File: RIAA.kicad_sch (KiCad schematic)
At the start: 114 parts, among them K1 G6K-2, P11 From Keyboard, P8 From main PCB, P9 From Wire, U1 OPA2134, U2 OPA2134, U3 LM317_TO-220, U4 LM337_TO-220, U5 OPA2134, U6 OPA2134, U7 LM317_TO-220

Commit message: WIP: Added gerber files.
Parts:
- added C108, C208: 10uF, Capacitor_THT:CP_Radial_D5.0mm_P2.50mm, symbol Device:C_Polarized_Small
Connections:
- net GND: now also C108.2, C208.2; no longer R110.2, R210.2
- new net: C208.1, R210.2
- new net: C108.1, R110.2
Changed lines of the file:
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@@
 	(wire
 		(pts
-			(xy 372.11 106.68) (xy 372.11 105.41)
-		)
-		(stroke
-			(width 0)
-			(type default)
-		)
-	)
-	(wire
-		(pts
 			(xy -83.82 73.66) (xy -87.63 73.66)
 		)
@@
 	(wire
 		(pts
+			(xy 58.42 180.34) (xy 64.77 180.34)
+		)
+		(stroke
+			(width 0)
+			(type default)
+		)
+	)
+	(wire
+		(pts
 			(xy 93.98 170.18) (xy 93.98 168.91)
 		)
@@
 	(wire
 		(pts
-			(xy 220.98 180.34) (xy 220.98 186.69)
+			(xy 190.5 113.03) (xy 190.5 115.57)
 		)
 		(stroke
@@
 	(wire
 		(pts
-			(xy 190.5 106.68) (xy 190.5 105.41)
+			(xy 220.98 180.34) (xy 220.98 186.69)
 		)
 		(stroke
@@
 	(wire
 		(pts
+			(xy 190.5 105.41) (xy 190.5 107.95)
+		)
+		(stroke
+			(width 0)
+			(type default)
+		)
+	)
+	(wire
+		(pts
 			(xy -228.6 49.53) (xy -222.25 49.53)
 		)
@@
 	(wire
 		(pts
+			(xy 372.11 111.76) (xy 372.11 114.3)
+		)
+		(stroke
+			(width 0)
+			(type default)
+		)
+	)
+	(wire
+		(pts
 			(xy 372.11 95.25) (xy 378.46 95.25)
 		)
@@
 	(wire
 		(pts
+			(xy 372.11 105.41) (xy 372.11 106.68)
+		)
+		(stroke
+			(width 0)
+			(type default)
+		)
+	)
+	(wire
+		(pts
 			(xy 393.7 149.86) (xy 393.7 162.56)
 		)
@@
 	(wire
 		(pts
-			(xy 58.42 180.34) (xy 64.77 180.34)
-		)
-		(stroke
-			(width 0)
-			(type default)
-		)
-	)
-	(wire
-		(pts
 			(xy 247.65 138.43) (xy 254 138.43)
 		)
@@
 				(size 1.27 1.27)
 			)
-			(justify left top)
+			(justify right top)
 		)
 	)
@@
 	)
 	(symbol
+		(lib_id "Device:C_Polarized_Small")
+		(at 372.11 109.22 0)
+		(unit 1)
+		(exclude_from_sim no)
+		(in_bom yes)
+		(on_board yes)
+		(dnp no)
+		(fields_autoplaced yes)
+		(property "Reference" "C208"
+			(at 374.65 107.4038 0)
+			(effects
+				(font
+					(size 1.27 1.27)
+				)
+				(justify left)
+			)
+		)
+		(property "Value" "10uF"
+			(at 374.65 109.9438 0)
+			(effects
+				(font
+					(size 1.27 1.27)
+				)
+				(justify left)
+			)
+		)
+		(property "Footprint" "Capacitor_THT:CP_Radial_D5.0mm_P2.50mm"
+			(at 372.11 109.22 0)
+			(effects
+				(font
+					(size 1.27 1.27)
+				)
+				(hide yes)
+			)
+		)
+		(property "Datasheet" "~"
+			(at 372.11 109.22 0)
+			(effects
+				(font
+					(size 1.27 1.27)
+				)
+				(hide yes)
+			)
+		)
+		(property "Description" "Polarized capacitor, small symbol"
+			(at 372.11 109.22 0)
+			(effects
+				(font
+					(size 1.27 1.27)
+				)
+				(hide yes)
+			)
+		)
+		(pin "2"
+		)
+		(pin "1"
+		)
+		(instances
+			(project "RIAA"
+				(path "/d42afdab-200b-47bd-9783-ae2fad19e73b"
+					(reference "C208")
+					(unit 1)
+				)
+			)
+		)
+	)
+	(symbol
 		(lib_id "Device:R")
 		(at 77.47 175.26 0)
@@
 	(symbol
 		(lib_id "power:GND")
-		(at 372.11 106.68 0)
+		(at 372.11 114.3 0)
+		(mirror y)
 		(unit 1)
 		(exclude_from_sim no)
@@
 		(on_board yes)
 		(dnp no)
-		(fields_autoplaced yes)
 		(property "Reference" "#PWR022"
-			(at 372.11 113.03 0)
+			(at 372.11 120.65 0)
 			(effects
 				(font
@@
 		)
 		(property "Value" "GND"
-			(at 372.11 111.76 0)
+			(at 372.11 119.38 0)
 			(effects
 				(font
@@
 		)
 		(property "Footprint" ""
-			(at 372.11 106.68 0)
+			(at 372.11 114.3 0)
 			(effects
 				(font
@@
 		)
 		(property "Datasheet" ""
-			(at 372.11 106.68 0)
+			(at 372.11 114.3 0)
 			(effects
 				(font
@@
 		)
 		(property "Description" "Power symbol creates a global label with name \"GND\" , ground"
-			(at 372.11 106.68 0)
+			(at 372.11 114.3 0)
 			(effects
 				(font
@@
 	(symbol
 		(lib_id "power:GND")
-		(at 190.5 106.68 0)
+		(at 190.5 115.57 0)
+		(mirror y)
 		(unit 1)
 		(exclude_from_sim no)
@@
 		(on_board yes)
 		(dnp no)
-		(fields_autoplaced yes)
 		(property "Reference" "#PWR015"
-			(at 190.5 113.03 0)
+			(at 190.5 121.92 0)
 			(effects
 				(font
@@
 		)
 		(property "Value" "GND"
-			(at 190.5 111.76 0)
+			(at 190.5 120.65 0)
 			(effects
 				(font
@@
 		)
 		(property "Footprint" ""
-			(at 190.5 106.68 0)
+			(at 190.5 115.57 0)
 			(effects
 				(font
@@
 		)
 		(property "Datasheet" ""
-			(at 190.5 106.68 0)
+			(at 190.5 115.57 0)
 			(effects
 				(font
@@
 		)
 		(property "Description" "Power symbol creates a global label with name \"GND\" , ground"
-			(at 190.5 106.68 0)
+			(at 190.5 115.57 0)
 			(effects
 				(font
@@
 					(unit 1)
 				)
+			)
+		)
+	)
+	(symbol
+		(lib_id "Device:C_Polarized_Small")
+		(at 190.5 110.49 0)
+		(mirror y)
+		(unit 1)
+		(exclude_from_sim no)
+		(in_bom yes)
+		(on_board yes)
+		(dnp no)
+		(property "Reference" "C108"
+			(at 187.96 108.6738 0)
+			(effects
+				(font
+					(size 1.27 1.27)
+				)
+				(justify left)
+			)
+		)
+		(property "Value" "10uF"
+			(at 187.96 111.2138 0)
+			(effects
+				(font
+					(size 1.27 1.27)
+				)
+				(justify left)
+			)
+		)
+		(property "Footprint" "Capacitor_THT:CP_Radial_D5.0mm_P2.50mm"
+			(at 190.5 110.49 0)
+			(effects
+				(font
+					(size 1.27 1.27)
+				)
+				(hide yes)
+			)
+		)
+		(property "Datasheet" "~"
+			(at 190.5 110.49 0)
+			(effects
+				(font
+					(size 1.27 1.27)
+				)
+				(hide yes)
+			)
+		)
+		(property "Description" "Polarized capacitor, small symbol"
+			(at 190.5 110.49 0)
+			(effects
+				(font
+					(size 1.27 1.27)
+				)
+				(hide yes)
+			)
+		)
+		(pin "2"
+		)
+		(pin "1"
+		)
+		(instances
+			(project "RIAA"
+				(path "/d42afdab-200b-47bd-9783-ae2fad19e73b"
+					(reference "C108")
+					(unit 1)
+				)

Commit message: WIP: Started on 3v3 voltage regulator for esp32.
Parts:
- added C34, C35, C36, C37: 22uF, Capacitor_THT:C_Rect_L4.6mm_W3.0mm_P2.50mm_MKS02_FKP02, symbol Device:C
- added L1: 4.7uH, symbol Device:L
- added R23, R25: 470, Resistor_THT:R_Axial_DIN0204_L3.6mm_D1.6mm_P7.62mm_Horizontal, symbol Device:R
- added R24: 6k8, Resistor_THT:R_Axial_DIN0204_L3.6mm_D1.6mm_P7.62mm_Horizontal, symbol Device:R
- added U10: AP63203WU, Package_TO_SOT_SMD:TSOT-23-6, symbol Regulator_Switching:AP63203WU
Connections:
- net 24VDC+: now also C34.2, U10.2 (EN), U10.3 (IN)
- net GND: now also C34.1, C35.1, C36.1, R24.1, U10.4 (GND)
- net R OUT: now also R25.1; no longer C207.2
- new net: C207.2, R23.2, R24.2
- new net: R23.1, R25.2
- new net: C37.1, U10.6 (BST)
- new net: C37.2, L1.1, U10.5 (SW)
- new net 3v3: C35.2, C36.2, L1.2, U10.1 (FB)

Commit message: WIP: Working on SMD version.
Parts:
- removed C34, C35, C36, C37: 22uF, Capacitor_THT:C_Rect_L4.6mm_W3.0mm_P2.50mm_MKS02_FKP02, symbol Device:C
- removed L1: 4.7uH, symbol Device:L
- removed R23, R25: 470, Resistor_THT:R_Axial_DIN0204_L3.6mm_D1.6mm_P7.62mm_Horizontal, symbol Device:R
- removed R24: 6k8, Resistor_THT:R_Axial_DIN0204_L3.6mm_D1.6mm_P7.62mm_Horizontal, symbol Device:R
- removed U10: AP63203WU, Package_TO_SOT_SMD:TSOT-23-6, symbol Regulator_Switching:AP63203WU
- BC1: footprint Package_TO_SOT_THT:TO-92 -> Package_TO_SOT_SMD:SOT-23_Handsoldering
- C204, C205: footprint Capacitor_THT:C_Rect_L4.6mm_W3.0mm_P2.50mm_MKS02_FKP02 -> Capacitor_THT:C_Rect_L7.2mm_W4.5mm_P5.00mm_FKS2_FKP2_MKS2_MKP2
- C206, C207, C208, C29, C30: footprint Capacitor_THT:CP_Radial_D5.0mm_P2.50mm -> Capacitor_SMD:CP_Elec_5x5.4
- C31: footprint Capacitor_THT:CP_Radial_D13.0mm_P7.50mm -> Capacitor_SMD:CP_Elec_8x6.9
- C33: footprint Capacitor_THT:CP_Radial_D8.0mm_P5.00mm -> Capacitor_SMD:CP_Elec_5x5.4
- D5, D6, D7, D8: footprint Diode_THT:D_A-405_P10.16mm_Horizontal -> Diode_SMD:D_MiniMELF
- R19, R20, R202, R203, R204, R205, R206, R208, R209, R21, R210, R211, R212, R22: footprint Resistor_THT:R_Axial_DIN0204_L3.6mm_D1.6mm_P7.62mm_Horizontal -> Resistor_SMD:R_1206_3216Metric_Pad1.30x1.75mm_HandSolder
- R207: footprint Resistor_THT:R_Axial_DIN0204_L3.6mm_D1.6mm_P7.62mm_Horizontal -> Resistor_SMD:R_1206_3216Metric_Pad1.30x1.75mm_HandSolder; LSCSL PN (none) -> C137334
- U7: footprint Package_TO_SOT_THT:TO-220-3_Horizontal_TabDown -> Package_TO_SOT_SMD:TO-252-3_TabPin2
- renumbered P11 to P10
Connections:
- net R OUT: now also C207.2

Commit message: WIP: Working on SMD.
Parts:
- C201, C202, C203: footprint Capacitor_THT:C_Rect_L4.6mm_W3.0mm_P2.50mm_MKS02_FKP02 -> Capacitor_THT:C_Rect_L7.2mm_W4.5mm_P5.00mm_FKS2_FKP2_MKS2_MKP2
- C27, C28, C32: footprint Capacitor_THT:C_Rect_L4.6mm_W3.0mm_P2.50mm_MKS02_FKP02 -> Capacitor_SMD:C_1206_3216Metric_Pad1.33x1.80mm_HandSolder
- C33: footprint Capacitor_SMD:CP_Elec_5x5.4 -> Capacitor_SMD:C_1206_3216Metric_Pad1.33x1.80mm_HandSolder
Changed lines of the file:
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@@
 	(title_block
 		(title "Beogram 4002 RIAA")
-		(date "2024-04-12")
+		(date "2026-27-01")
 		(rev "0.1")
 		(company "LEICHT.IO")
@@
 			)
 		)
-		(property "Footprint" "Capacitor_THT:C_Rect_L4.6mm_W3.0mm_P2.50mm_MKS02_FKP02"
+		(property "Footprint" "Capacitor_THT:C_Rect_L7.2mm_W4.5mm_P5.00mm_FKS2_FKP2_MKS2_MKP2"
 			(at 261.9248 82.55 0)
 			(effects
@@
 			)
 		)
-		(property "Footprint" "Capacitor_THT:C_Rect_L4.6mm_W3.0mm_P2.50mm_MKS02_FKP02"
+		(property "Footprint" "Capacitor_SMD:C_1206_3216Metric_Pad1.33x1.80mm_HandSolder"
 			(at 24.4348 77.47 0)
 			(effects
@@
 			)
 		)
-		(property "Footprint" "Capacitor_THT:C_Rect_L4.6mm_W3.0mm_P2.50mm_MKS02_FKP02"
+		(property "Footprint" "Capacitor_THT:C_Rect_L7.2mm_W4.5mm_P5.00mm_FKS2_FKP2_MKS2_MKP2"
 			(at 293.0652 114.3 0)
 			(effects
@@
 			)
 		)
-		(property "Footprint" "Capacitor_THT:C_Rect_L4.6mm_W3.0mm_P2.50mm_MKS02_FKP02"
+		(property "Footprint" "Capacitor_SMD:C_1206_3216Metric_Pad1.33x1.80mm_HandSolder"
 			(at 40.9448 77.47 0)
 			(effects
@@
 			)
 		)
-		(property "Footprint" "Capacitor_SMD:CP_Elec_5x5.4"
+		(property "Footprint" "Capacitor_SMD:C_1206_3216Metric_Pad1.33x1.80mm_HandSolder"
 			(at 256.54 138.43 0)
 			(effects
@@
 			)
 		)
-		(property "Footprint" "Capacitor_THT:C_Rect_L4.6mm_W3.0mm_P2.50mm_MKS02_FKP02"
+		(property "Footprint" "Capacitor_THT:C_Rect_L7.2mm_W4.5mm_P5.00mm_FKS2_FKP2_MKS2_MKP2"
 			(at 302.26 96.8248 0)
 			(effects
@@
 			)
 		)
-		(property "Footprint" "Capacitor_THT:C_Rect_L4.6mm_W3.0mm_P2.50mm_MKS02_FKP02"
+		(property "Footprint" "Capacitor_SMD:C_1206_3216Metric_Pad1.33x1.80mm_HandSolder"
 			(at 128.5748 167.64 0)
 			(effects

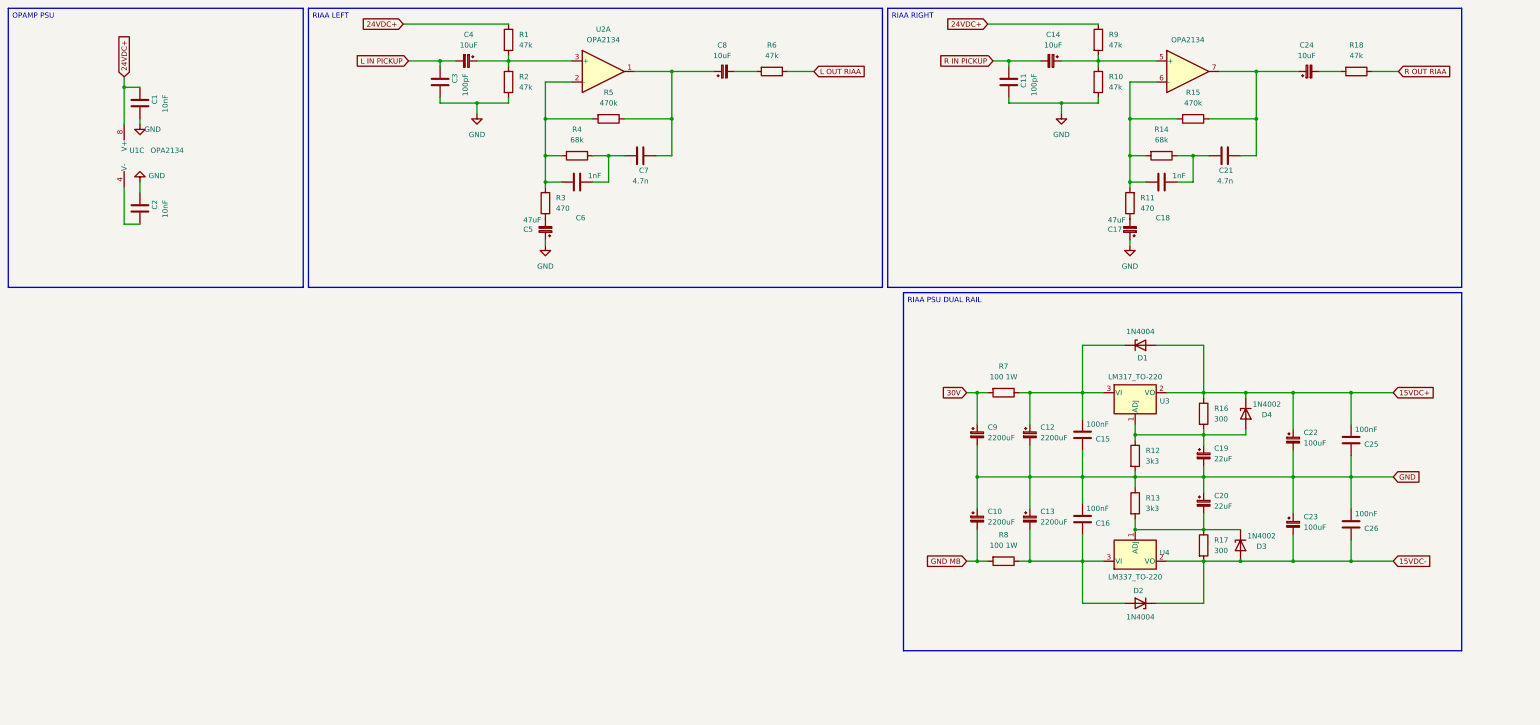
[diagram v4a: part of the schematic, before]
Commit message: WIP: Working on SMD version.
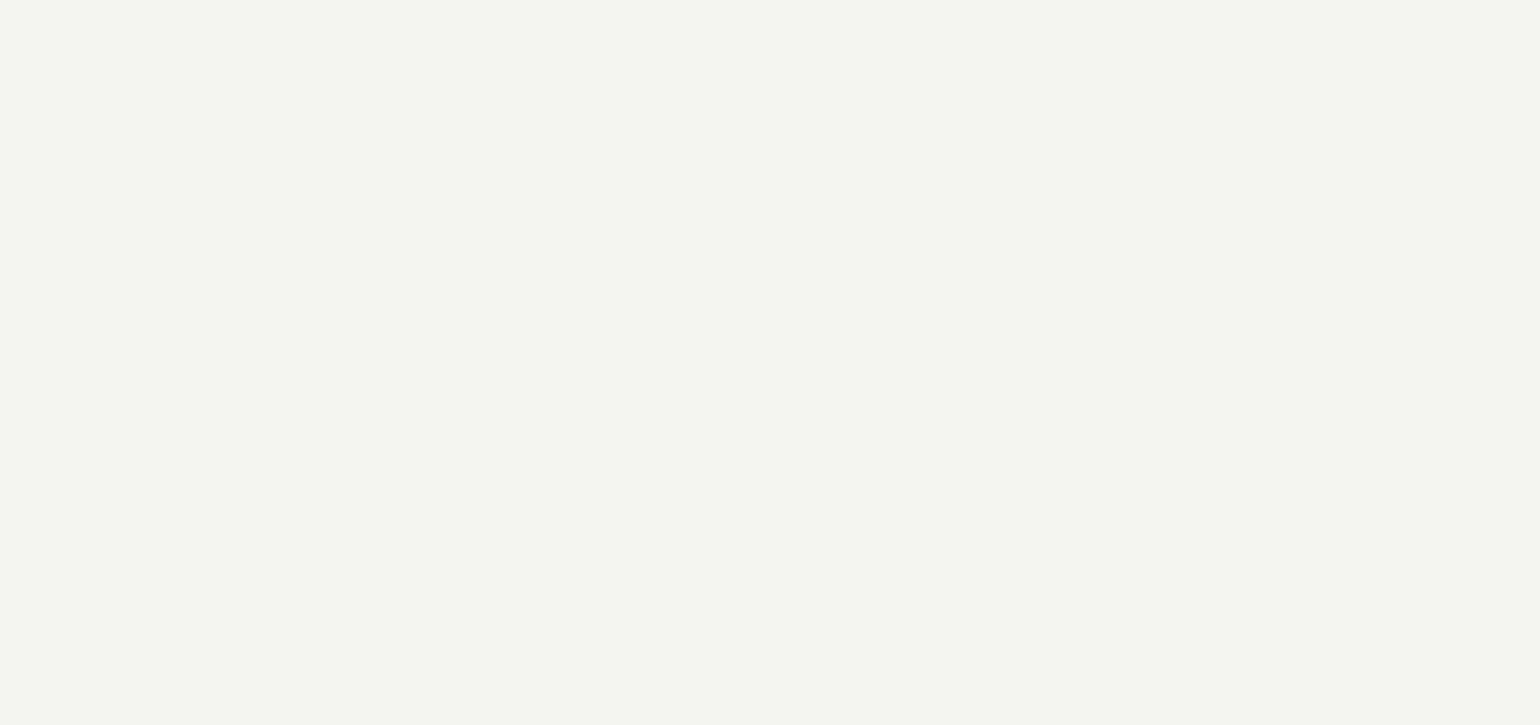
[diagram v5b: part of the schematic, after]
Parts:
- removed C1, C2: 10nF, Capacitor_THT:C_Rect_L4.6mm_W3.0mm_P2.50mm_MKS02_FKP02, symbol Device:C
- removed C10, C12, C13, C9: 2200uF, Capacitor_THT:CP_Radial_D12.5mm_P5.00mm, symbol Device:C_Polarized_Small
- removed C11, C3: 100pF, Capacitor_THT:C_Rect_L4.6mm_W3.0mm_P2.50mm_MKS02_FKP02, symbol Device:C
- removed C14, C24, C4, C8: 10uF, Capacitor_THT:CP_Radial_D4.0mm_P2.00mm, symbol Device:C_Polarized_Small
- removed C15, C16, C25, C26: 100nF, Capacitor_THT:C_Rect_L4.6mm_W3.0mm_P2.50mm_MKS02_FKP02, symbol Device:C
- removed C17, C5: 47uF, Capacitor_THT:CP_Radial_D4.0mm_P2.00mm, symbol Device:C_Polarized_Small
- removed C18, C6: 1nF, Capacitor_THT:C_Rect_L4.6mm_W3.0mm_P2.50mm_MKS02_FKP02, symbol Device:C
- removed C19, C20: 22uF, Capacitor_THT:CP_Radial_D12.5mm_P5.00mm, symbol Device:C_Polarized_Small
- removed C21, C7: 4.7n, Capacitor_THT:C_Rect_L4.6mm_W3.0mm_P2.50mm_MKS02_FKP02, symbol Device:C
- removed C22, C23: 100uF, Capacitor_THT:CP_Radial_D12.5mm_P5.00mm, symbol Device:C_Polarized_Small
- removed D1, D2: 1N4004, Diode_THT:D_A-405_P10.16mm_Horizontal, symbol Device:D_Zener
- removed D3, D4: 1N4002, Diode_THT:D_A-405_P10.16mm_Horizontal, symbol Device:D_Zener
- removed R1, R10, R18, R2, R6, R9: 47k, Resistor_THT:R_Axial_DIN0204_L3.6mm_D1.6mm_P7.62mm_Horizontal, symbol Device:R
- removed R11, R3: 470, Resistor_THT:R_Axial_DIN0204_L3.6mm_D1.6mm_P7.62mm_Horizontal, symbol Device:R
- removed R12, R13: 3k3, Resistor_THT:R_Axial_DIN0204_L3.6mm_D1.6mm_P7.62mm_Horizontal, symbol Device:R
- removed R14, R4: 68k, Resistor_THT:R_Axial_DIN0204_L3.6mm_D1.6mm_P7.62mm_Horizontal, symbol Device:R
- removed R15, R5: 470k, Resistor_THT:R_Axial_DIN0204_L3.6mm_D1.6mm_P7.62mm_Horizontal, symbol Device:R
- removed R16, R17: 300, Resistor_THT:R_Axial_DIN0204_L3.6mm_D1.6mm_P7.62mm_Horizontal, symbol Device:R
- removed R7, R8: 100 1W, Resistor_THT:R_Axial_DIN0204_L3.6mm_D1.6mm_P7.62mm_Horizontal, symbol Device:R
- removed U1: OPA2134, Package_SO:SOIC-8_3.9x4.9mm_P1.27mm, symbol Amplifier_Operational:LM358
- removed U2: OPA2134, OPA2134:D8, symbol Amplifier_Operational:OPA2134
- removed U3: LM317_TO-220, Package_TO_SOT_THT:TO-220-3_Horizontal_TabDown, symbol Regulator_Linear:LM317_TO-220
- removed U4: LM337_TO-220, Package_TO_SOT_THT:TO-220-3_Horizontal_TabDown, symbol Regulator_Linear:LM317_TO-220
- C101: footprint Capacitor_THT:C_Rect_L4.6mm_W3.0mm_P2.50mm_MKS02_FKP02 -> Capacitor_THT:C_Rect_L7.2mm_W4.5mm_P5.00mm_FKS2_FKP2_MKS2_MKP2
- R102, R103, R110: footprint Resistor_THT:R_Axial_DIN0204_L3.6mm_D1.6mm_P7.62mm_Horizontal -> Resistor_SMD:R_1206_3216Metric_Pad1.30x1.75mm_HandSolder
- RV1: footprint Potentiometer_SMD:Potentiometer_ACP_CA6-VSMD_Vertical_Hole -> Potentiometer_SMD:Potentiometer_Bourns_3314J_Vertical; LSCS PN (none) -> C6083402

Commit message: WIP: Finishing up SMD version.
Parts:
- C102, C103, C104, C105: footprint Capacitor_THT:C_Rect_L4.6mm_W3.0mm_P2.50mm_MKS02_FKP02 -> Capacitor_THT:C_Rect_L7.2mm_W4.5mm_P5.00mm_FKS2_FKP2_MKS2_MKP2
- C106, C107, C108: footprint Capacitor_THT:CP_Radial_D5.0mm_P2.50mm -> Capacitor_SMD:CP_Elec_5x5.4
- R104, R105, R106, R107, R108, R109, R111, R112: footprint Resistor_THT:R_Axial_DIN0204_L3.6mm_D1.6mm_P7.62mm_Horizontal -> Resistor_SMD:R_1206_3216Metric_Pad1.30x1.75mm_HandSolder
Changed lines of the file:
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@@
 			)
 		)
-		(property "Footprint" "Capacitor_THT:C_Rect_L4.6mm_W3.0mm_P2.50mm_MKS02_FKP02"
+		(property "Footprint" "Capacitor_THT:C_Rect_L7.2mm_W4.5mm_P5.00mm_FKS2_FKP2_MKS2_MKP2"
 			(at 165.1 81.5848 0)
 			(effects
@@
 			)
 		)
-		(property "Footprint" "Resistor_THT:R_Axial_DIN0204_L3.6mm_D1.6mm_P7.62mm_Horizontal"
+		(property "Footprint" "Resistor_SMD:R_1206_3216Metric_Pad1.30x1.75mm_HandSolder"
 			(at 179.832 88.9 90)
 			(effects
@@
 			)
 		)
-		(property "Footprint" "Resistor_THT:R_Axial_DIN0204_L3.6mm_D1.6mm_P7.62mm_Horizontal"
+		(property "Footprint" "Resistor_SMD:R_1206_3216Metric_Pad1.30x1.75mm_HandSolder"
 			(at 124.46 90.932 90)
 			(effects
@@
 			)
 		)
-		(property "Footprint" "Resistor_THT:R_Axial_DIN0204_L3.6mm_D1.6mm_P7.62mm_Horizontal"
+		(property "Footprint" "Resistor_SMD:R_1206_3216Metric_Pad1.30x1.75mm_HandSolder"
 			(at 140.97 80.772 90)
 			(effects
@@
 			)
 		)
-		(property "Footprint" "Capacitor_THT:CP_Radial_D5.0mm_P2.50mm"
+		(property "Footprint" "Capacitor_SMD:CP_Elec_5x5.4"
 			(at 87.63 80.01 0)
 			(effects
@@
 			)
 		)
-		(property "Footprint" "Capacitor_THT:C_Rect_L4.6mm_W3.0mm_P2.50mm_MKS02_FKP02"
+		(property "Footprint" "Capacitor_THT:C_Rect_L7.2mm_W4.5mm_P5.00mm_FKS2_FKP2_MKS2_MKP2"
 			(at 166.6748 85.09 0)
 			(effects
@@
 			)
 		)
-		(property "Footprint" "Resistor_THT:R_Axial_DIN0204_L3.6mm_D1.6mm_P7.62mm_Horizontal"
+		(property "Footprint" "Resistor_SMD:R_1206_3216Metric_Pad1.30x1.75mm_HandSolder"
 			(at 179.832 77.47 90)
 			(effects
@@
 			)
 		)
-		(property "Footprint" "Resistor_THT:R_Axial_DIN0204_L3.6mm_D1.6mm_P7.62mm_Horizontal"
+		(property "Footprint" "Resistor_SMD:R_1206_3216Metric_Pad1.30x1.75mm_HandSolder"
 			(at 110.49 90.932 90)
 			(effects
@@
 			)
 		)
-		(property "Footprint" "Resistor_THT:R_Axial_DIN0204_L3.6mm_D1.6mm_P7.62mm_Horizontal"
+		(property "Footprint" "Resistor_SMD:R_1206_3216Metric_Pad1.30x1.75mm_HandSolder"
 			(at 153.162 88.9 90)
 			(effects
@@
 			)
 		)
-		(property "Footprint" "Resistor_THT:R_Axial_DIN0204_L3.6mm_D1.6mm_P7.62mm_Horizontal"
+		(property "Footprint" "Resistor_SMD:R_1206_3216Metric_Pad1.30x1.75mm_HandSolder"
 			(at 102.362 101.6 90)
 			(effects
@@
 			)
 		)
-		(property "Footprint" "Resistor_THT:R_Axial_DIN0204_L3.6mm_D1.6mm_P7.62mm_Horizontal"
+		(property "Footprint" "Resistor_SMD:R_1206_3216Metric_Pad1.30x1.75mm_HandSolder"
 			(at 200.66 93.472 90)
 			(effects
@@
 			)
 		)
-		(property "Footprint" "Capacitor_THT:CP_Radial_D5.0mm_P2.50mm"
+		(property "Footprint" "Capacitor_SMD:CP_Elec_5x5.4"
 			(at 190.5 110.49 0)
 			(effects
@@
 			)
 		)
-		(property "Footprint" "Capacitor_THT:CP_Radial_D5.0mm_P2.50mm"
+		(property "Footprint" "Capacitor_SMD:CP_Elec_5x5.4"
 			(at 213.36 85.09 0)
 			(effects
@@
 			)
 		)
-		(property "Footprint" "Capacitor_THT:C_Rect_L4.6mm_W3.0mm_P2.50mm_MKS02_FKP02"
+		(property "Footprint" "Capacitor_THT:C_Rect_L7.2mm_W4.5mm_P5.00mm_FKS2_FKP2_MKS2_MKP2"
 			(at 114.3 96.8248 0)
 			(effects
@@
 			)
 		)
-		(property "Footprint" "Capacitor_THT:C_Rect_L4.6mm_W3.0mm_P2.50mm_MKS02_FKP02"
+		(property "Footprint" "Capacitor_THT:C_Rect_L7.2mm_W4.5mm_P5.00mm_FKS2_FKP2_MKS2_MKP2"
 			(at 105.1052 114.3 0)
 			(effects
